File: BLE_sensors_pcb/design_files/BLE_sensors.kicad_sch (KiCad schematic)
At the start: 8 parts, among them J1 Conn_ARM_SWD_TagConnect_TC203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, J2 Conn_01x02, U4 ME54BS01

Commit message: Added a capasitor to me54bs01 pwr supply and added gerbers and schematic
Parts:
- added C14: 0.1u, Capacitor_SMD:C_0603_1608Metric, symbol Device:C_Small
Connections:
- net +3V3: now also C14.1
- net GND: now also C14.2
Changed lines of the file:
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@@
 	)
 	(junction
-		(at 85.09 104.14)
+		(at 68.58 104.14)
+		(diameter 0)
+		(color 0 0 0 0)
+	)
+	(junction
+		(at 121.92 128.27)
 		(diameter 0)
 		(color 0 0 0 0)
@@
 	(wire
 		(pts
-			(xy 110.49 105.41) (xy 125.73 105.41)
+			(xy 121.92 129.54) (xy 121.92 128.27)
+		)
+		(stroke
+			(width 0)
+			(type default)
+		)
+	)
+	(wire
+		(pts
+			(xy 93.98 105.41) (xy 125.73 105.41)
 		)
 		(stroke
@@
 	(wire
 		(pts
+			(xy 121.92 134.62) (xy 121.92 135.89)
+		)
+		(stroke
+			(width 0)
+			(type default)
+		)
+	)
+	(wire
+		(pts
 			(xy 204.47 115.57) (xy 204.47 116.84)
 		)
@@
 	(wire
 		(pts
-			(xy 116.84 128.27) (xy 125.73 128.27)
+			(xy 121.92 128.27) (xy 125.73 128.27)
+		)
+		(stroke
+			(width 0)
+			(type default)
+		)
+	)
+	(wire
+		(pts
+			(xy 116.84 128.27) (xy 121.92 128.27)
 		)
 		(stroke
@@
 	(wire
 		(pts
-			(xy 85.09 102.87) (xy 85.09 104.14)
+			(xy 68.58 102.87) (xy 68.58 104.14)
 		)
 		(stroke
@@
 	(wire
 		(pts
-			(xy 85.09 104.14) (xy 85.09 109.22)
+			(xy 68.58 104.14) (xy 68.58 109.22)
 		)
 		(stroke
@@
 	(wire
 		(pts
-			(xy 92.71 109.22) (xy 85.09 109.22)
+			(xy 76.2 109.22) (xy 68.58 109.22)
 		)
 		(stroke
@@
 	(wire
 		(pts
-			(xy 85.09 104.14) (xy 92.71 104.14)
+			(xy 68.58 104.14) (xy 76.2 104.14)
 		)
 		(stroke
@@
 	(wire
 		(pts
-			(xy 110.49 107.95) (xy 125.73 107.95)
+			(xy 93.98 107.95) (xy 125.73 107.95)
 		)
 		(stroke
@@
 	)
 	(label "SCL"
-		(at 119.38 107.95 180)
+		(at 111.76 107.95 180)
 		(effects
 			(font
@@
 	)
 	(label "SDA"
-		(at 119.38 105.41 180)
+		(at 111.76 105.41 180)
 		(effects
 			(font
@@
 	(symbol
 		(lib_id "power:+3V3")
-		(at 85.09 102.87 0)
+		(at 68.58 102.87 0)
 		(unit 1)
 		(exclude_from_sim no)
@@
 		(dnp no)
 		(property "Reference" "#PWR054"
-			(at 85.09 106.68 0)
+			(at 68.58 106.68 0)
 			(effects
 				(font
@@
 		)
 		(property "Value" "+3V3"
-			(at 88.392 101.346 0)
+			(at 71.882 101.346 0)
 			(effects
 				(font
@@
 		)
 		(property "Footprint" ""
-			(at 85.09 102.87 0)
+			(at 68.58 102.87 0)
 			(effects
 				(font
@@
 		)
 		(property "Datasheet" ""
-			(at 85.09 102.87 0)
+			(at 68.58 102.87 0)
 			(effects
 				(font
@@
 		)
 		(property "Description" "Power symbol creates a global label with name \"+3V3\""
-			(at 85.09 102.87 0)
+			(at 68.58 102.87 0)
 			(effects
 				(font
@@
 	)
 	(symbol
+		(lib_id "power:GND")
+		(at 121.92 135.89 0)
+		(unit 1)
+		(exclude_from_sim no)
+		(in_bom yes)
+		(on_board yes)
+		(dnp no)
+		(property "Reference" "#PWR034"
+			(at 121.92 142.24 0)
+			(effects
+				(font
+					(size 1.27 1.27)
+				)
+				(hide yes)
+			)
+		)
+		(property "Value" "GND"
+			(at 121.92 139.446 0)
+			(effects
+				(font
+					(size 1.27 1.27)
+				)
+			)
+		)
+		(property "Footprint" ""
+			(at 121.92 135.89 0)
+			(effects
+				(font
+					(size 1.27 1.27)
+				)
+				(hide yes)
+			)
+		)
+		(property "Datasheet" ""
+			(at 121.92 135.89 0)
+			(effects
+				(font
+					(size 1.27 1.27)
+				)
+				(hide yes)
+			)
+		)
+		(property "Description" "Power symbol creates a global label with name \"GND\" , ground"
+			(at 121.92 135.89 0)
+			(effects
+				(font
+					(size 1.27 1.27)
+				)
+				(hide yes)
+			)
+		)
+		(pin "1"
+		)
+		(instances
+			(project "BLE_sensors"
+				(path "/06b47d3c-6b7b-411b-8755-cae193722202"
+					(reference "#PWR034")
+					(unit 1)
+				)
+			)
+		)
+	)
+	(symbol
 		(lib_id "power:+3V3")
 		(at 172.72 115.57 0)
@@
 	)
 	(symbol
+		(lib_id "Device:C_Small")
+		(at 121.92 132.08 0)
+		(unit 1)
+		(exclude_from_sim no)
+		(in_bom yes)
+		(on_board yes)
+		(dnp no)
+		(property "Reference" "C14"
+			(at 125.222 130.81 0)
+			(effects
+				(font
+					(size 1.27 1.27)
+				)
+			)
+		)
+		(property "Value" "0.1u"
+			(at 126.238 132.842 0)
+			(effects
+				(font
+					(size 1.27 1.27)
+				)
+			)
+		)
+		(property "Footprint" "Capacitor_SMD:C_0603_1608Metric"
+			(at 121.92 132.08 0)
+			(effects
+				(font
+					(size 1.27 1.27)
+				)
+				(hide yes)
+			)
+		)
+		(property "Datasheet" "~"
+			(at 121.92 132.08 0)
+			(effects
+				(font
+					(size 1.27 1.27)
+				)
+				(hide yes)
+			)
+		)
+		(property "Description" "Unpolarized capacitor, small symbol"
+			(at 121.92 132.08 0)
+			(effects
+				(font
+					(size 1.27 1.27)
+				)
+				(hide yes)
+			)
+		)
+		(pin "2"
+		)
+		(pin "1"
+		)
+		(instances
+			(project "BLE_sensors"
+				(path "/06b47d3c-6b7b-411b-8755-cae193722202"
+					(reference "C14")
+					(unit 1)
+				)
+			)
+		)
+	)
+	(symbol
 		(lib_id "power:+3V3")
 		(at 63.5 71.12 0)
@@
 	)
 	(sheet
-		(at 92.71 101.6)
+		(at 76.2 101.6)
 		(size 17.78 10.16)
 		(exclude_from_sim no)
@@
 		)
 		(property "Sheetname" "Temp Sensor"
-			(at 92.71 100.8884 0)
+			(at 76.2 100.8884 0)
 			(effects
 				(font
@@
 		)
 		(property "Sheetfile" "Temp_Sensor.kicad_sch"
-			(at 92.71 112.3446 0)
+			(at 76.2 112.3446 0)
 			(effects
 				(font
@@
 		)
 		(pin "SCL" input
-			(at 110.49 107.95 0)
+			(at 93.98 107.95 0)
 			(effects
 				(font
@@
 		)
 		(pin "SDA" input
-			(at 110.49 105.41 0)
+			(at 93.98 105.41 0)
 			(effects
 				(font
@@
 		)
 		(pin "Vdd" input
-			(at 92.71 104.14 180)
+			(at 76.2 104.14 180)
 			(effects
 				(font
@@
 		)
 		(pin "Vddio" input
-			(at 92.71 109.22 180)
+			(at 76.2 109.22 180)
 			(effects
 				(font

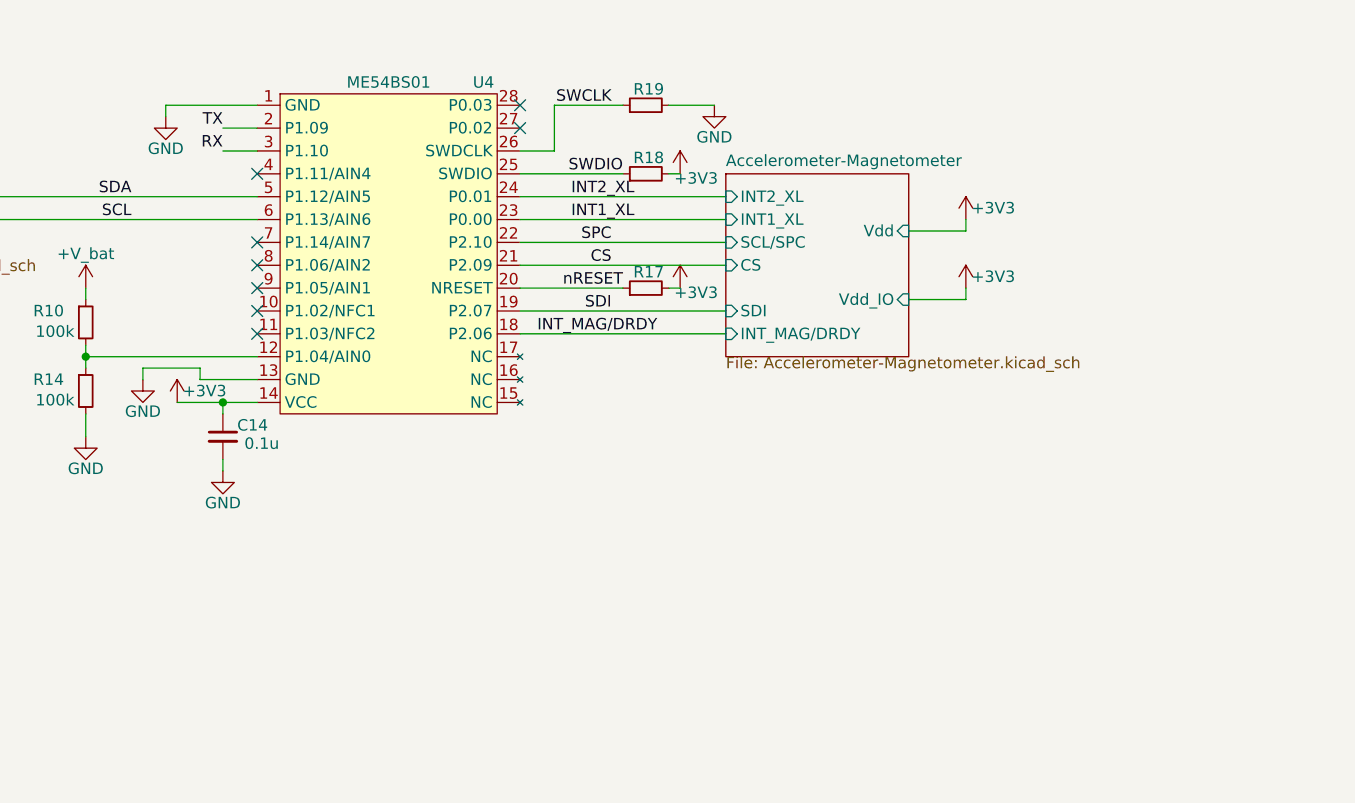
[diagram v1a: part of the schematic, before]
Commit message: fixed spi
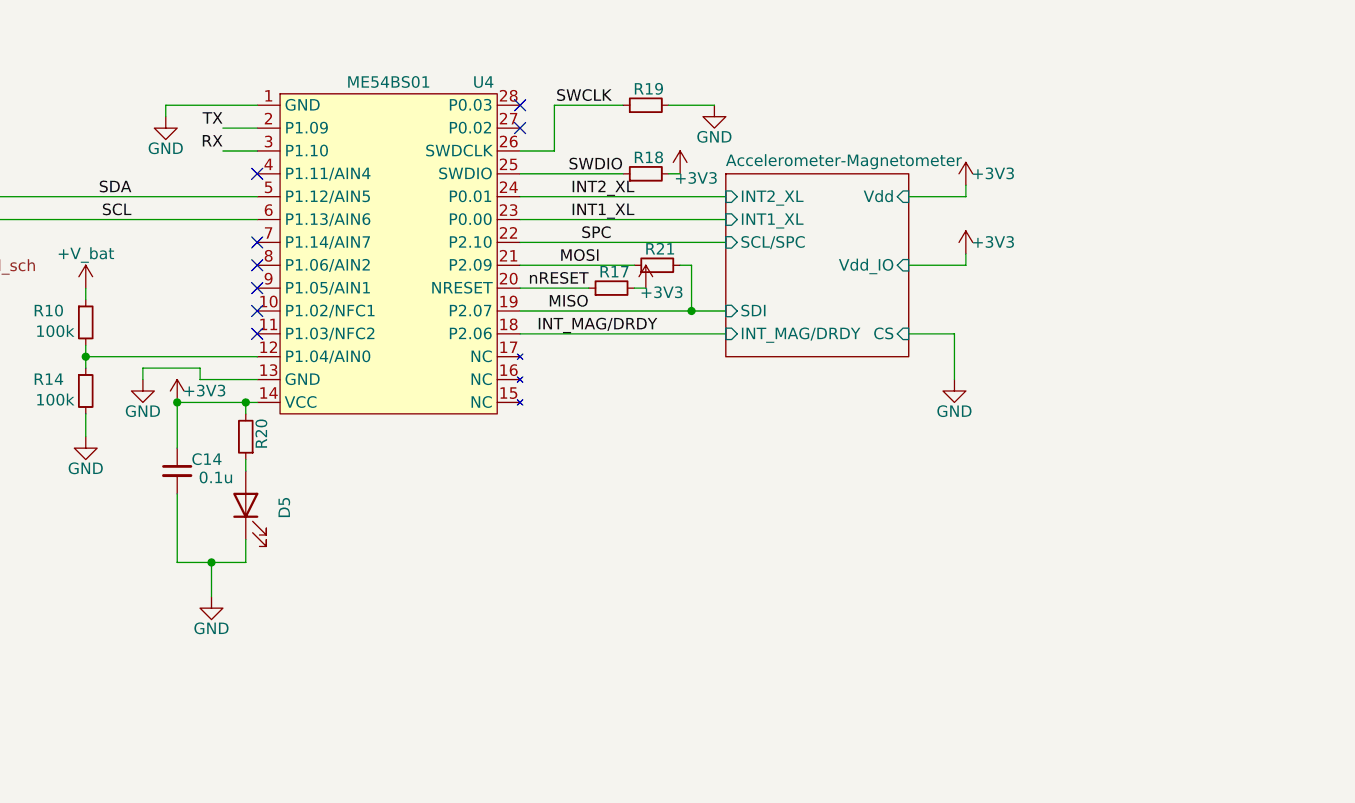
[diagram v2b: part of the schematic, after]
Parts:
- added D5: LED, LED_SMD:LED_0603_1608Metric, symbol Device:LED
- added R20: 470R, Resistor_SMD:R_0603_1608Metric, symbol Device:R_Small
- added R21: 10k, Resistor_SMD:R_0603_1608Metric, symbol Device:R_Small
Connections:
- net +3V3: now also R20.2
- net GND: now also D5.1 (K)
- net CS renamed MOSI
- net MOSI: now also R21.1
- net SDI renamed MISO
- net MISO: now also R21.2
- new net: D5.2 (A), R20.1
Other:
- moved on the sheet: C14, R17

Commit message: Added pdf
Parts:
- removed D5: LED, LED_SMD:LED_0603_1608Metric, symbol Device:LED
- removed R20: 470R, Resistor_SMD:R_0603_1608Metric, symbol Device:R_Small
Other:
- moved on the sheet: C14, R21
